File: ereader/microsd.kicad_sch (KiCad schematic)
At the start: 43 parts, among them J2 DM3AT-SF-PEJM5, U17 TPS22950CDDCR, U18 TPS3808G30DBVR, U19 SN74LVC1G97DBVR, U20 SN74LVC1G97DBVR, U21 TMUX1511RSVR, U22 TMUX1511RSVR

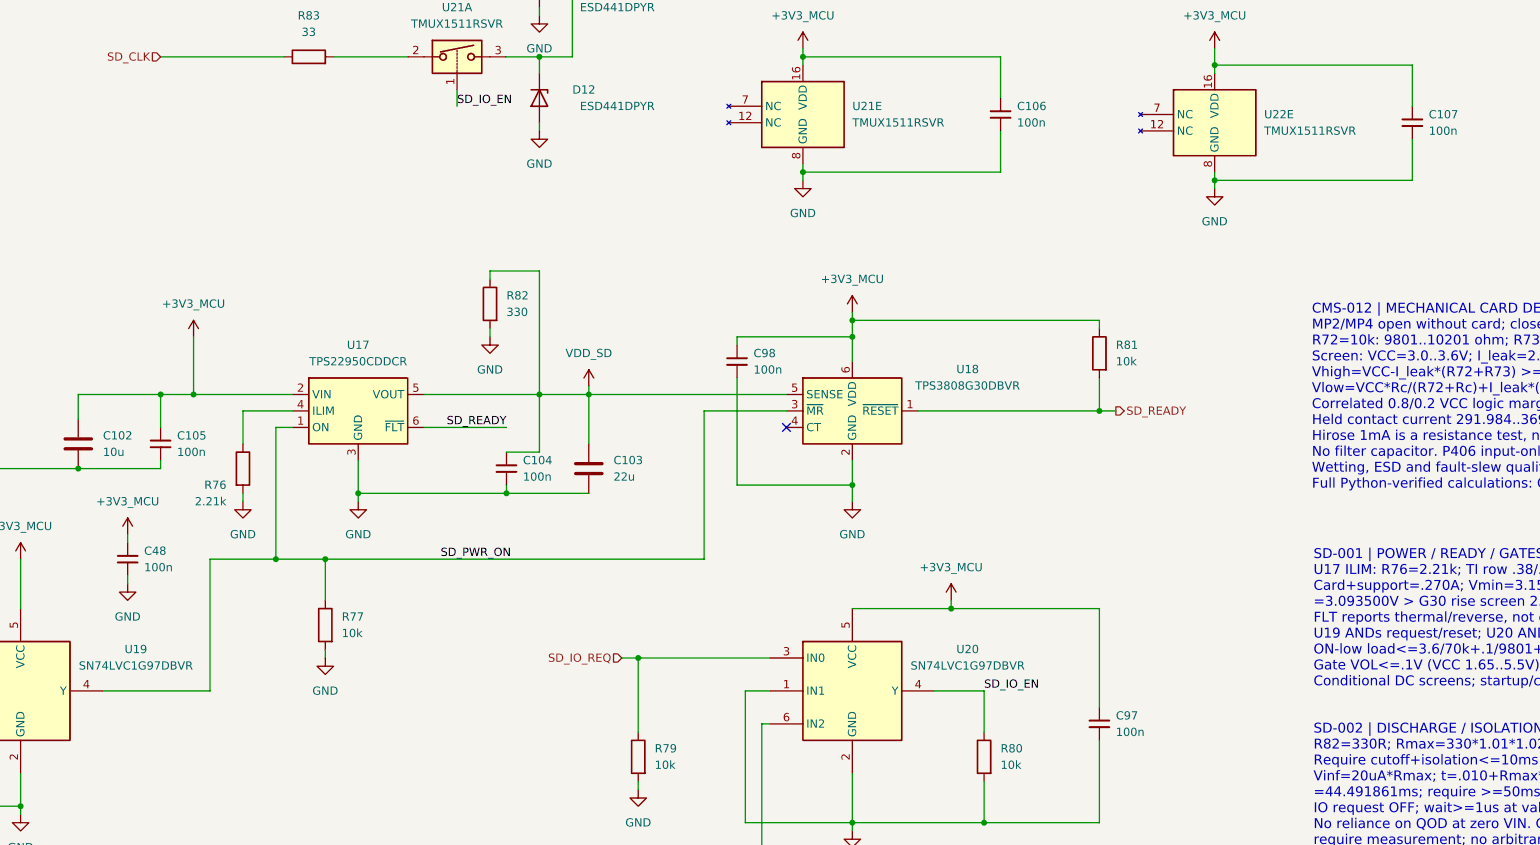
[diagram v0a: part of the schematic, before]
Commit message: WIP: integrate orientation sensor and refresh schematic review exports
Add LIS2DW12 host wiring and sourced passives, revise held-supply discharge calculations, document camera and capacitance screens, and refresh standard capacitor caches. Include reviewed 14-page PDF and reconciled native BOM. ERC remains 111 errors and 11 warnings; electrical design is incomplete. Refs #21.
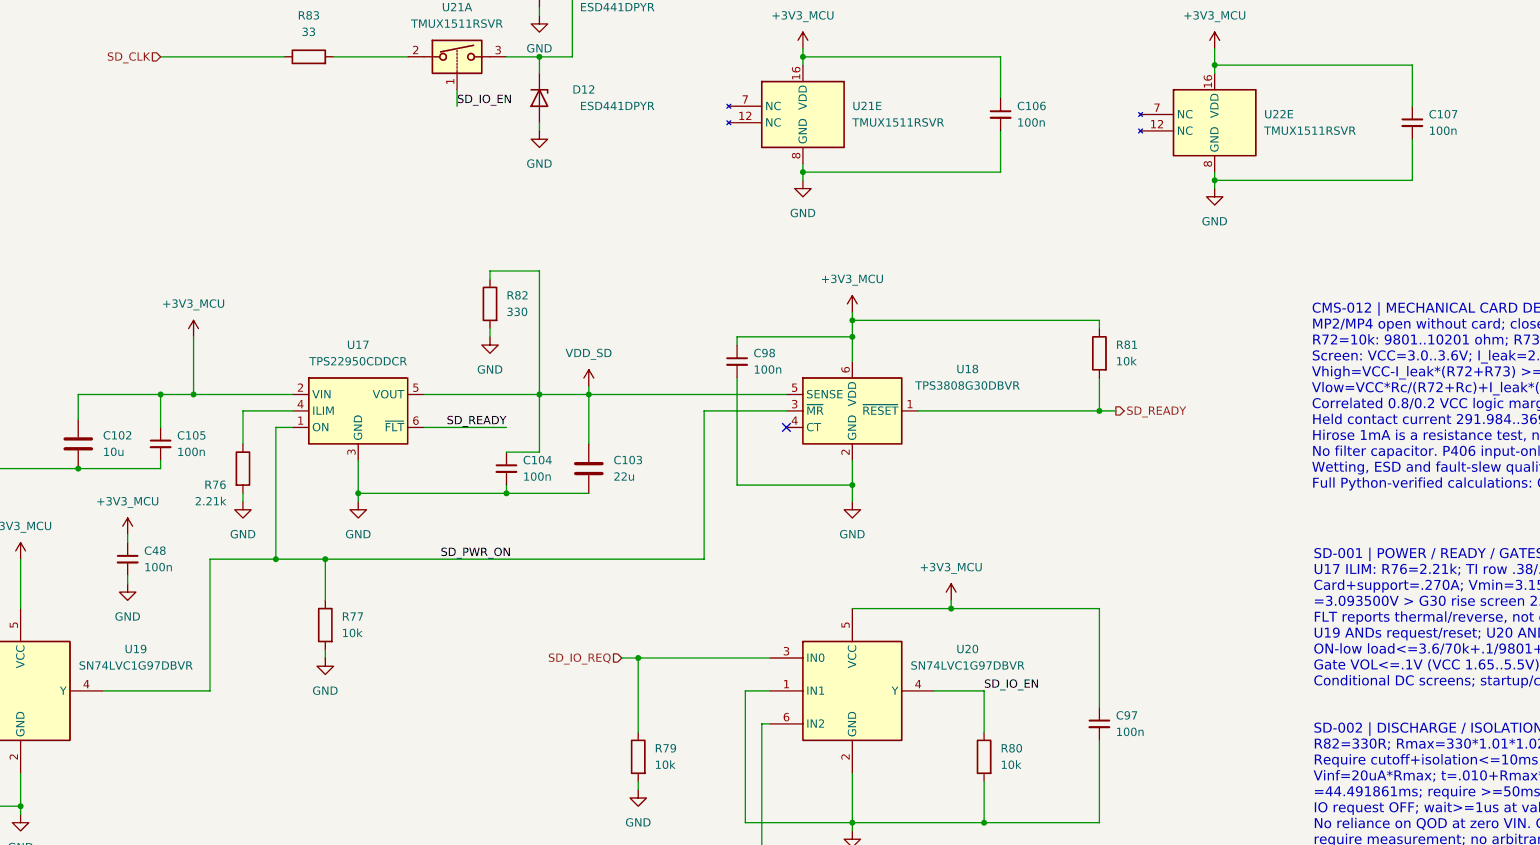
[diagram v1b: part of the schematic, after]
